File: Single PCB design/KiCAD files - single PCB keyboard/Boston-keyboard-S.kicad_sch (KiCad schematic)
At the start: 577 parts, among them J705 TYPE-C-31-M12_13, J706 Conn_ARM_JTAG_SWD_10, Q701 DTC123J, Q702 AO4406AL, SW1 MXSwitch, SW10 MXSwitch, SW100 MXSwitch, SW101 MXSwitch, SW102 MXSwitch, SW103 MXSwitch, SW104 MXSwitch, SW105-1 MXSwitch, SW105-2 MXSwitch, SW106 MXSwitch, SW107 MXSwitch, SW108 MXSwitch, SW109 MXSwitch, SW11 MXSwitch, SW110 MXSwitch, SW111 MXSwitch, SW112 MXSwitch, SW113 MXSwitch, SW114 MXSwitch, SW115 MXSwitch, SW116 MXSwitch, SW117 MXSwitch, SW118 MXSwitch, SW119 MXSwitch, SW12 MXSwitch, SW120 MXSwitch, SW121 MXSwitch, SW122 MXSwitch, SW123 MXSwitch, SW124-1 MXSwitch, SW124-2 MXSwitch, SW125 MXSwitch, SW126 Rotary_Encoder_Switch_Chassis, SW127 MXSwitch, SW13 MXSwitch, SW14 MXSwitch, SW15 MXSwitch, SW16 MXSwitch, SW17 MXSwitch, SW18 MXSwitch, SW19 MXSwitch, SW2 MXSwitch, SW20 MXSwitch, SW200 SW_Push, SW21 MXSwitch, SW22 MXSwitch, SW23 MXSwitch, SW24 MXSwitch, SW25 MXSwitch, SW26 MXSwitch, SW27 MXSwitch, SW28 MXSwitch, SW29 MXSwitch, SW3 MXSwitch, SW30 MXSwitch, SW31 MXSwitch, SW32 MXSwitch, SW33 MXSwitch, SW34 MXSwitch, SW35 MXSwitch, SW36 MXSwitch, SW37 MXSwitch, SW38 MXSwitch, SW39 MXSwitch, SW4-1 MXSwitch, SW4-2 MXSwitch, SW40 MXSwitch, SW41 MXSwitch, SW42 MXSwitch, SW43 MXSwitch, SW44 MXSwitch, SW45 MXSwitch, SW46 MXSwitch, SW47 MXSwitch, SW48 MXSwitch, SW49 MXSwitch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

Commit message: Updated RGB LED location
Now moved to daughterboard, with the goal to underglow the encoder knob.
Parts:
- removed H1, H2: MountingHole, MountingHole:MountingHole_3.2mm_M3_ISO7380, symbol Mechanical:MountingHole
- removed LED301: LED_RAGB, LED_THT:LED_D5.0mm-4_RGB, symbol Device:LED_RAGB
- removed R711: 100, Resistor_SMD:R_0805_2012Metric_Pad1.15x1.40mm_HandSolder, symbol Device:R
- removed U1: WS2811, Package_SO:SOP-8_3.9x4.9mm_P1.27mm, symbol Driver_LED:WS2811
- added C1: 47uF, Capacitor_SMD:C_1206_3216Metric, symbol Device:C
- added J701: Conn_01x02_Female, Connector_PinSocket_2.54mm:PinSocket_1x02_P2.54mm_Vertical, symbol Connector:Conn_01x02_Female
- added J702: Conn_01x03_Female, Connector_PinSocket_2.54mm:PinSocket_1x03_P2.54mm_Vertical, symbol Connector:Conn_01x03_Female
- added LED702: NeoPixel_THT, LED_THT:LED_D5.0mm-4_RGB, symbol LED:NeoPixel_THT
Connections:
- net +3V3: now also C712.1; no longer C704.1
- net +5V: now also C704.1, C1.1, J702.1 (Pin_1), LED702.3 (VDD)
- net GND: now also C1.2, J701.1 (Pin_1), J701.2 (Pin_2), J702.3 (Pin_3), LED702.2 (GND)
- net DI: now reaches R710.1
- net DI: now also J702.2 (Pin_2), LED702.4 (DIN)
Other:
- note added: "Bottom position"
- moved on the sheet: C704, R710, U705

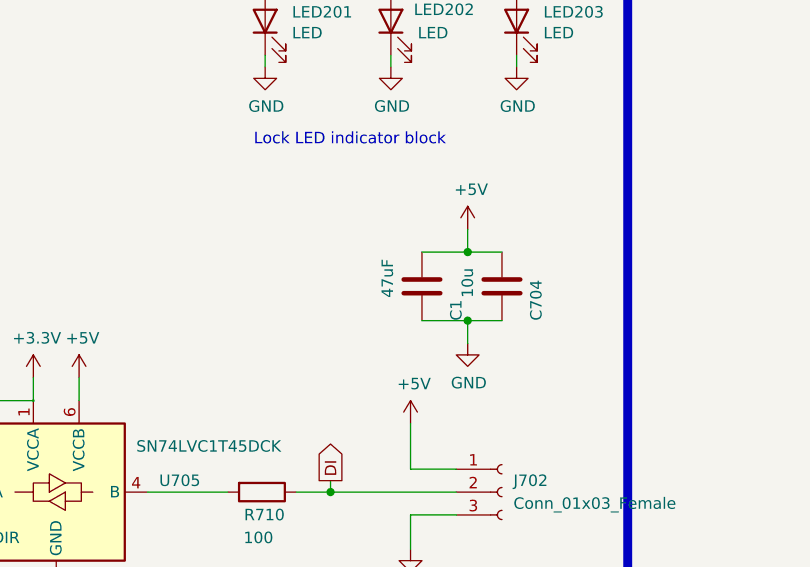
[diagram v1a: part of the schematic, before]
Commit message: Silkscreen changes
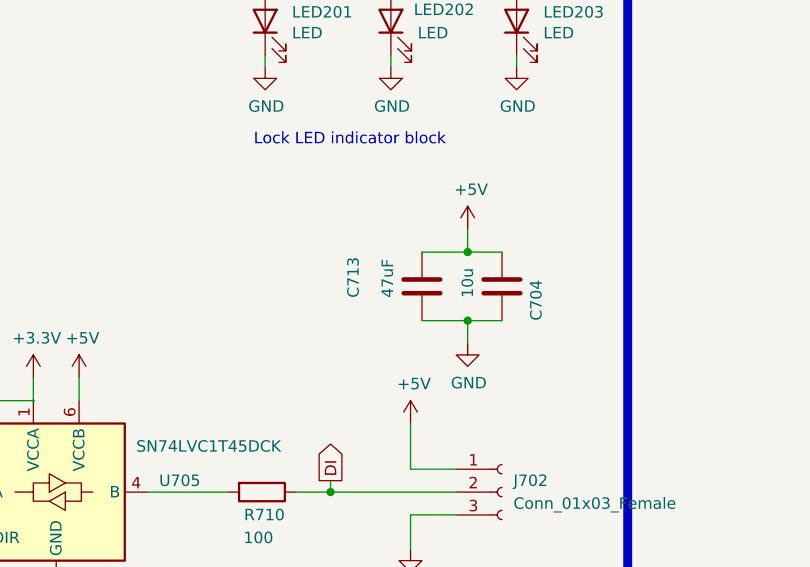
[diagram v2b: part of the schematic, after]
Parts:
- renumbered C1 to C713
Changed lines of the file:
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@@
   (symbol (lib_id "Device:C") (at 440.69 407.67 0) (unit 1)
     (in_bom yes) (on_board yes)
-    (property "Reference" "C1" (id 0) (at 444.5 411.48 90)
+    (property "Reference" "C713" (id 0) (at 433.07 408.94 90)
       (effects (font (size 1.27 1.27)) (justify left))
     )
@@
       (reference "#PWR0704") (unit 1)
     )
-    (path "/a3070f96-f593-482a-93df-5b1621502866"
-      (reference "C1") (unit 1)
-    )
     (path "/00000000-0000-0000-0000-00005ed38979"
       (reference "C701") (unit 1)
@@
       (reference "C712") (unit 1)
     )
+    (path "/a3070f96-f593-482a-93df-5b1621502866"
+      (reference "C713") (unit 1)
+    )
     (path "/00000000-0000-0000-0000-00005dd5be69"

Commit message: Flipped encoder footprint
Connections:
- net Col1: now also SW126.S2; no longer SW126.S1
- net EncA: now also R708.1, U701.6 (PF1); no longer R709.1, U701.2 (PC13)
- net EncB: now also R709.1, U701.2 (PC13); no longer R708.1, U701.6 (PF1)
- net at D126.2 (A): now also SW126.S1; no longer SW126.S2
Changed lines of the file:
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@@
   (page 1 1)
   (paper "E")
-  (junction (at 34.29 52.07) (diameter 0.3048) (color 0 0 0 0))
+  (junction (at 34.29 46.99) (diameter 0) (color 0 0 0 0))
   (junction (at 34.29 81.28) (diameter 0.3048) (color 0 0 0 0))
   (junction (at 34.29 120.65) (diameter 0.3048) (color 0 0 0 0))
@@
   (junction (at 1074.42 33.02) (diameter 0.3048) (color 0 0 0 0))
   (junction (at 1084.58 33.02) (diameter 0.3048) (color 0 0 0 0))
-  (no_connect (at 826.77 86.36))
-  (no_connect (at 986.79 129.54))
   (no_connect (at 986.79 132.08))
   (no_connect (at 826.77 83.82))
+  (no_connect (at 986.79 129.54))
+  (no_connect (at 826.77 86.36))
   (wire (pts (xy 25.4 35.56) (xy 39.37 35.56))
     (stroke (width 0) (type solid) (color 0 0 0 0))
@@
     (stroke (width 0) (type solid) (color 0 0 0 0))
   )
-  (wire (pts (xy 34.29 30.48) (xy 34.29 52.07))
+  (wire (pts (xy 34.29 30.48) (xy 34.29 46.99))
+    (stroke (width 0) (type solid) (color 0 0 0 0))
+  )
+  (wire (pts (xy 34.29 46.99) (xy 34.29 81.28))
     (stroke (width 0) (type solid) (color 0 0 0 0))
   )
-  (wire (pts (xy 34.29 52.07) (xy 34.29 81.28))
+  (wire (pts (xy 34.29 46.99) (xy 41.91 46.99))
     (stroke (width 0) (type solid) (color 0 0 0 0))
   )
@@
     (stroke (width 0) (type solid) (color 0 0 0 0))
   )
-  (wire (pts (xy 39.37 46.99) (xy 39.37 44.45))
-    (stroke (width 0) (type solid) (color 0 0 0 0))
+  (wire (pts (xy 39.37 44.45) (xy 39.37 52.07))
+    (stroke (width 0.1524) (type solid) (color 0 0 0 0))
   )
   (wire (pts (xy 39.37 416.56) (xy 46.99 416.56))
@@
     (stroke (width 0) (type solid) (color 0 0 0 0))
   )
-  (wire (pts (xy 41.91 46.99) (xy 39.37 46.99))
-    (stroke (width 0) (type solid) (color 0 0 0 0))
-  )
-  (wire (pts (xy 41.91 52.07) (xy 34.29 52.07))
+  (wire (pts (xy 41.91 52.07) (xy 39.37 52.07))
     (stroke (width 0) (type solid) (color 0 0 0 0))
   )
@@
     (effects (font (size 1.27 1.27)) (justify left))
   )
-  (global_label "EncB" (shape input) (at 816.61 205.74 180)
+  (global_label "EncA" (shape input) (at 816.61 205.74 180)
     (effects (font (size 1.27 1.27)) (justify right))
   )
-  (global_label "EncA" (shape input) (at 816.61 210.82 180)
+  (global_label "EncB" (shape input) (at 816.61 210.82 180)
     (effects (font (size 1.27 1.27)) (justify right))
   )

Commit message: Unflipped encoder, ended up editing the footprint
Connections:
- net Col1: now also SW126.S1; no longer SW126.S2
- net EncA: now also R709.1, U701.2 (PC13); no longer R708.1, U701.6 (PF1)
- net EncB: now also R708.1, U701.6 (PF1); no longer R709.1, U701.2 (PC13)
- net at D126.2 (A): now also SW126.S2; no longer SW126.S1
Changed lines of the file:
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@@
   (page 1 1)
   (paper "E")
-  (junction (at 34.29 46.99) (diameter 0) (color 0 0 0 0))
+  (junction (at 34.29 52.07) (diameter 0.3048) (color 0 0 0 0))
   (junction (at 34.29 81.28) (diameter 0.3048) (color 0 0 0 0))
   (junction (at 34.29 120.65) (diameter 0.3048) (color 0 0 0 0))
@@
     (stroke (width 0) (type solid) (color 0 0 0 0))
   )
-  (wire (pts (xy 34.29 30.48) (xy 34.29 46.99))
+  (wire (pts (xy 34.29 30.48) (xy 34.29 52.07))
     (stroke (width 0) (type solid) (color 0 0 0 0))
   )
-  (wire (pts (xy 34.29 46.99) (xy 34.29 81.28))
-    (stroke (width 0) (type solid) (color 0 0 0 0))
-  )
-  (wire (pts (xy 34.29 46.99) (xy 41.91 46.99))
+  (wire (pts (xy 34.29 52.07) (xy 34.29 81.28))
     (stroke (width 0) (type solid) (color 0 0 0 0))
   )
@@
     (stroke (width 0) (type solid) (color 0 0 0 0))
   )
-  (wire (pts (xy 39.37 44.45) (xy 39.37 52.07))
-    (stroke (width 0.1524) (type solid) (color 0 0 0 0))
+  (wire (pts (xy 39.37 46.99) (xy 39.37 44.45))
+    (stroke (width 0) (type solid) (color 0 0 0 0))
   )
   (wire (pts (xy 39.37 416.56) (xy 46.99 416.56))
@@
     (stroke (width 0) (type solid) (color 0 0 0 0))
   )
-  (wire (pts (xy 41.91 52.07) (xy 39.37 52.07))
+  (wire (pts (xy 41.91 46.99) (xy 39.37 46.99))
+    (stroke (width 0) (type solid) (color 0 0 0 0))
+  )
+  (wire (pts (xy 41.91 52.07) (xy 34.29 52.07))
     (stroke (width 0) (type solid) (color 0 0 0 0))
   )
@@
     (effects (font (size 1.27 1.27)) (justify left))
   )
-  (global_label "EncA" (shape input) (at 816.61 205.74 180)
+  (global_label "EncB" (shape input) (at 816.61 205.74 180)
     (effects (font (size 1.27 1.27)) (justify right))
   )
-  (global_label "EncB" (shape input) (at 816.61 210.82 180)
+  (global_label "EncA" (shape input) (at 816.61 210.82 180)
     (effects (font (size 1.27 1.27)) (justify right))
   )

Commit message: Added WKL and 1.5u bottom row, added grounding hole, updated silkscreens
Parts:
- added H1: MountingHole_Pad, MountingHole:MountingHole_3.5mm_Pad_Via, symbol Mechanical:MountingHole_Pad
- added LED20-2, LED39-2, LED6-2, LED64-2, LED78-2: LED, LED_THT:LED_D3.0mm_Clear, symbol Device:LED
- added SW20-2, SW6-2, SW64-2, SW78-2: MXSwitch, acheron_MX:MX150, symbol Boston-keyboard-rescue:MXSwitch-Acheron
- added SW39-2: MXSwitch, acheron_MX:MX700, symbol Boston-keyboard-rescue:MXSwitch-Acheron
- renumbered LED20 to LED20-1, LED39 to LED39-1, LED6 to LED6-1, LED64 to LED64-1, LED78 to LED78-1, SW20 to SW20-1, SW39 to SW39-1, SW6 to SW6-1, SW64 to SW64-1, SW78 to SW78-1
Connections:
- net Col1: now also SW6-2.1 (Col)
- net Col10: now also SW64-2.1 (Col)
- net Col12: now also SW78-2.1 (Col)
- net Col3: now also SW20-2.1 (Col)
- net Col6: now also SW39-2.1 (Col)
- net GND: now also H1.1
- net LED_switch: now also LED20-2.1 (K), LED39-2.1 (K), LED6-2.1 (K), LED64-2.1 (K), LED78-2.1 (K)
- net at D6.2 (A), SW6-1.2 (Row): now also SW6-2.2 (Row)
- net at D20.2 (A), SW20-1.2 (Row): now also SW20-2.2 (Row)
- net at D39.2 (A), SW39-1.2 (Row): now also SW39-2.2 (Row)
- net at D64.2 (A), SW64-1.2 (Row): now also SW64-2.2 (Row)
- net at D78.2 (A), SW78-1.2 (Row): now also SW78-2.2 (Row)
- net at LED6-1.2 (A), R6.2: now also LED6-2.2 (A)
- net at LED78-1.2 (A), R78.2: now also LED78-2.2 (A)
- net at LED39-1.2 (A), R39.2: now also LED39-2.2 (A)
- net at LED20-1.2 (A), R20.2: now also LED20-2.2 (A)
- net at LED64-1.2 (A), R64.2: now also LED64-2.2 (A)
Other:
- note added: "6.25u Space"
- note added: "7u Space"
- note added: "Hole for grounding"
- note added: "LAlt (1.25u)"
- note added: "LAlt (1.5u)"
- note added: "LCtrl (1.25u)"
- note added: "LCtrl (1.5u)"
- note added: "RAlt (1.5u)"
- note added: "RAlt (1u)"
- note added: "RCtrl (1.5u)"
- note added: "RCtrl (1u)"
- note removed: "B1Spc"
- note removed: "LAlt"
- note removed: "LCtrl"
- note removed: "RAlt"
- note removed: "RCtrl"
- moved on the sheet: LED10, LED100, LED102, LED103, LED104, LED106, LED107, LED108, LED11, LED110, LED111, LED112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

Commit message: Added UFQFPN48 alternate footprint for STM32; removed vias from underneath pads
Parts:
- added D128, D129: 1N4148, acheronComponents:D_SOD-123, symbol Diode:1N4148
- added LED128, LED129, LED39-3: LED, LED_THT:LED_D3.0mm_Clear, symbol Device:LED
- added R128, R129: 47, Resistor_SMD:R_0805_2012Metric_Pad1.15x1.40mm_HandSolder, symbol Device:R
- added SW128: MXSwitch, acheron_MX:MX225, symbol Boston-keyboard-rescue:MXSwitch-Acheron
- added SW129: MXSwitch, acheron_MX:MX275, symbol Boston-keyboard-rescue:MXSwitch-Acheron
- added SW39-3: MXSwitch, acheron_MX:MX125, symbol Boston-keyboard-rescue:MXSwitch-Acheron
- added UA701: STM32F072CBUx, Package_DFN_QFN:QFN-48-1EP_7x7mm_P0.5mm_EP5.6x5.6mm, symbol MCU_ST_STM32F0:STM32F072CBUx
- C713: value 47uF -> 22uF
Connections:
- net +3V3: now also R128.1, R129.1, UA701.1 (VBAT), UA701.24 (VDD), UA701.36 (VDDIO2), UA701.48 (VDD), UA701.9 (VDDA)
- net BOOT0: now also UA701.44 (BOOT0)
- net Col1: now also UA701.21 (PB10)
- net Col10: now also UA701.38 (PA15)
- net Col11: now also UA701.39 (PB3)
- net Col12: now also UA701.40 (PB4)
- net Col13: now also UA701.43 (PB7)
- net Col14: now also UA701.45 (PB8)
- net Col15: now also UA701.46 (PB9)
- net Col16: now also UA701.3 (PC14)
- net Col17: now also UA701.4 (PC15)
- net Col18: now also UA701.5 (PF0)
- net Col19: now also UA701.13 (PA3)
- net Col2: now also UA701.22 (PB11)
- net Col3: now also UA701.25 (PB12)
- net Col4: now also UA701.26 (PB13)
- net Col5: now also SW128.1 (Col), UA701.27 (PB14)
- net Col6: now also SW39-3.1 (Col), UA701.28 (PB15)
- net Col7: now also UA701.29 (PA8)
- net Col8: now also SW129.1 (Col), UA701.30 (PA9)
- net Col9: now also UA701.31 (PA10)
- net D+: now also UA701.33 (PA12)
- net D-: now also UA701.32 (PA11)
- net EncA: now also UA701.2 (PC13)
- net EncB: now also UA701.6 (PF1)
- net GND: now also UA701.23 (VSS), UA701.35 (VSS), UA701.47 (VSS), UA701.49 (VSS), UA701.8 (VSSA)
- net LED_PWM: now also UA701.16 (PA6)
- net LED_switch: now also LED128.1 (K), LED129.1 (K), LED39-3.1 (K)
- net NRST: now also UA701.7 (NRST)
- net RGBLED: now also UA701.15 (PA5)
- net Row1: now also UA701.41 (PB5)
- net Row2: now also UA701.42 (PB6)
- net Row3: now also UA701.17 (PA7)
- net Row4: now also UA701.18 (PB0)
- net Row5: now also UA701.19 (PB1)
- net Row6: now also UA701.20 (PB2)
- net Row7: now also D128.1 (K), D129.1 (K), UA701.14 (PA4)
- net SWCLK: now also UA701.37 (PA14)
- net SWDIO: now also UA701.34 (PA13)
- net at D39.2 (A), SW39-1.2 (Row), SW39-2.2 (Row): now also SW39-3.2 (Row)
- net at LED39-1.2 (A), LED39-2.2 (A), R39.2: now also LED39-3.2 (A)
- net at R200.2, U701.12 (PA2): now also UA701.12 (PA2)
- net at R201.2, U701.11 (PA1): now also UA701.11 (PA1)
- net at R202.2, U701.10 (PA0): now also UA701.10 (PA0)
- new net: D129.2 (A), SW129.2 (Row)
- new net: LED129.2 (A), R129.2
- new net: D128.2 (A), SW128.2 (Row)
- new net: LED128.2 (A), R128.2
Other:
- note added: "1.25u Split Space Mid"
- note added: "ISP header"
- note added: "LQFP-48"
- note added: "Microcontroller"
- note added: "RGBLED stuff"
- note added: "Split Space Left"
- note added: "Split Space Right"
- note added: "UFQFPN48 alternate"
- moved on the sheet: C701, C703, C704, C706, C711, C712, C713, D701, F701, J701, J702, J706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

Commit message: Updated bottom
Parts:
- C701, C706, C711: footprint Capacitor_SMD:C_1210_3225Metric_Pad1.42x2.65mm_HandSolder -> Capacitor_SMD:C_1206_3216Metric_Pad1.42x1.75mm_HandSolder
- C713: value 22uF -> 10u
- R1, R10, R100, R101, R102, R103, R104, R105-1, R105-2, R106, R107, R108, R109, R11, R110, R111, R112, R113, R114, R115, R116, R117, R118, R119, R12, R120, R121, R122, R123, R124-1, R124-2, R125, R127, R128, R129, R13, R14, R15, R16, R17, R18, R19, R2, R20, R21, R22, R23, R24, R25, R26, R27, R28, R29, R3, R30, R31, R32, R33, R34, R35, R36, R37, R38, R39, R4, R40, R41, R42, R43, R44, R45, R46, R47, R48, R49, R5-1, R5-2, R50, R51, R52, R53, R54, R55, R56, R57, R58, R59, R6, R60, R61, R62, R63, R64, R65, R66, R67, R68, R69, R7, R70, R71, R72, R73, R74, R75, R76, R77, R78, R79, R8, R80, R81, R82, R83, R84, R85, R86, R87, R88-1, R88-2, R89, R9, R90-1, R90-2, R91, R92, R93, R94, R95, R96, R97, R98, R99: value 47 -> 100

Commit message: Final revisions before sending to JLCPCB on 9/18/2020
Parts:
- C704, C713: footprint Capacitor_SMD:C_1206_3216Metric -> Capacitor_SMD:C_1206_3216Metric_Pad1.42x1.75mm_HandSolder
- C715: renamed from CRST1; footprint Capacitor_SMD:C_1206_3216Metric -> Capacitor_SMD:C_1206_3216Metric_Pad1.42x1.75mm_HandSolder
- renumbered CUSB1 to C714, LED105-1 to LED1051, LED105-2 to LED1052, LED124-1 to LED1241, LED124-2 to LED1242, LED20-1 to LED2001, LED20-2 to LED2002, LED39-1 to LED391, LED39-2 to LED392, LED39-3 to LED393, LED4-1 to LED401, LED4-2 to LED402, LED5-1 to LED501, LED5-2 to LED502, LED6-1 to LED601, LED6-2 to LED602, LED64-1 to LED641, LED64-2 to LED642, LED78-1 to LED781, LED78-2 to LED782, LED88-1 to LED881, LED88-2 to LED882, LED90-1 to LED901, LED90-2 to LED902, R105-1 to R1051, R105-2 to R1052, R124-1 to R1241, R124-2 to R1242, R5-1 to R501, R5-2 to R502, R88-1 to R881, R88-2 to R882, R90-1 to R901, R90-2 to R902
